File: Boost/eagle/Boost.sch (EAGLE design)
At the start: 17 parts, among them X1 22-23-2051

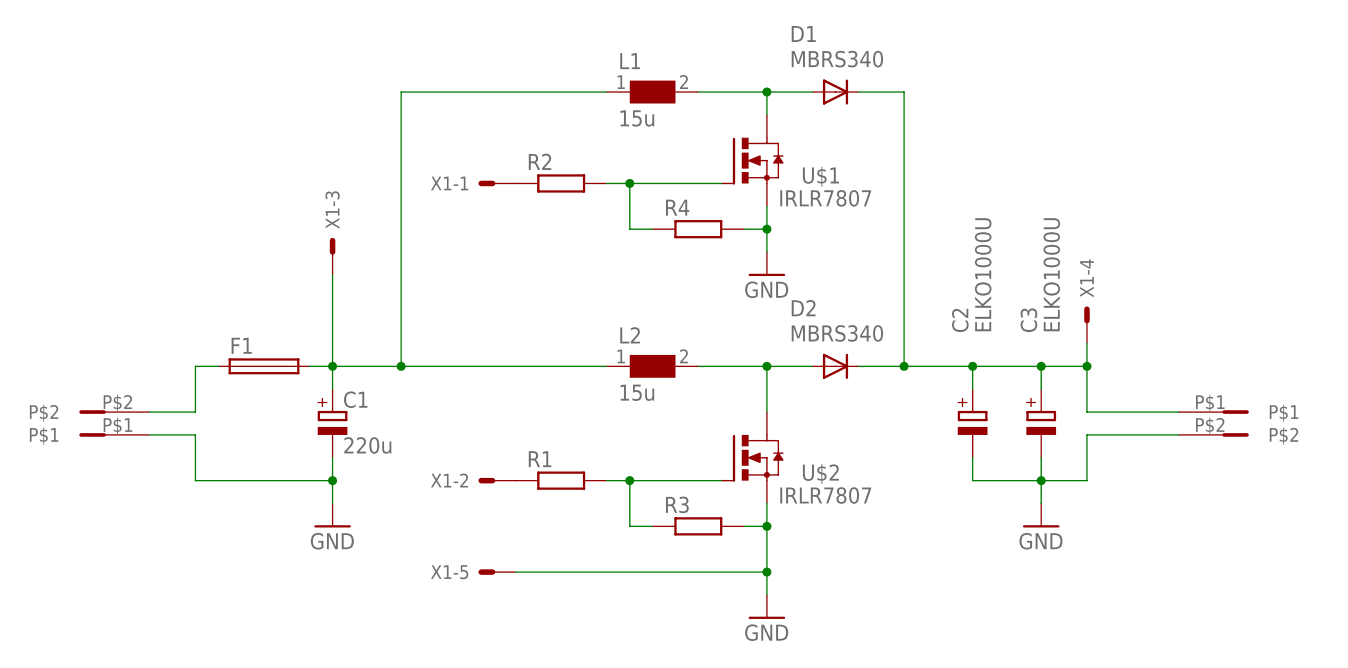
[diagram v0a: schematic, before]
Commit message: updated boost converter layout
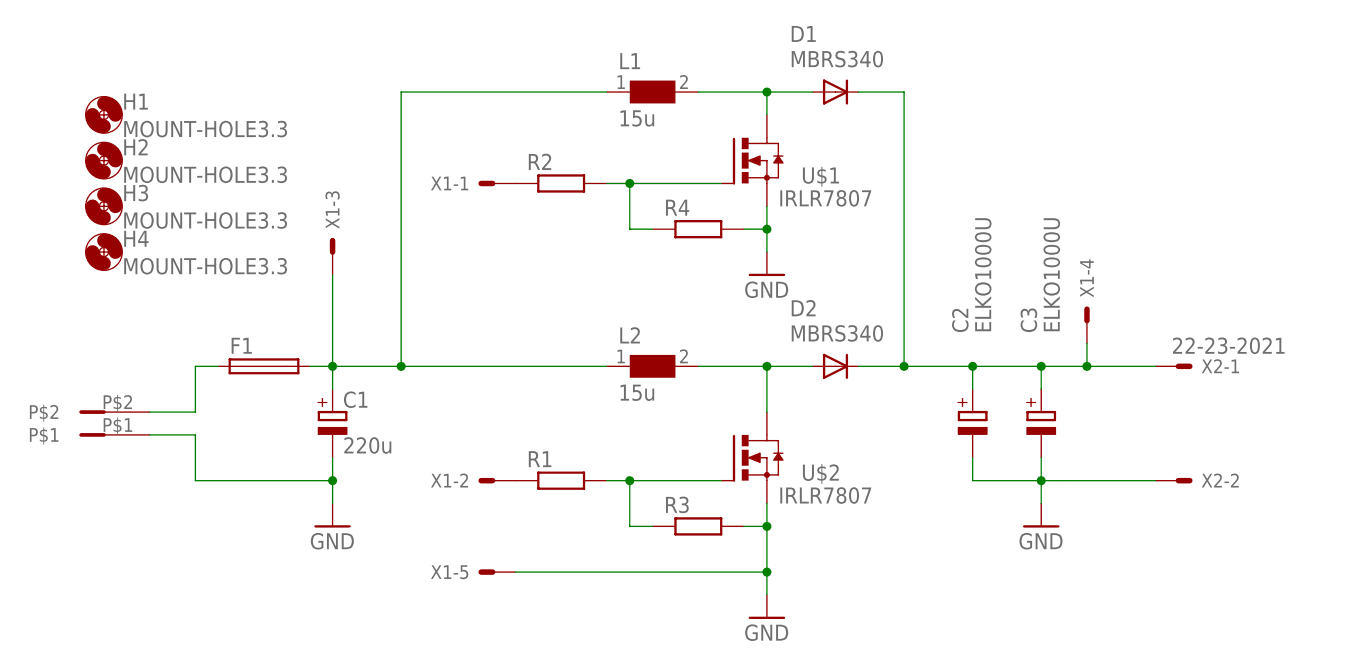
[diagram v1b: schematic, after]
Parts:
- removed U$4: RIACON-2, ppst002:RIACON-2
- added H1, H2, H3, H4: MOUNT-HOLE3.3, holes:MOUNT-HOLE3.3
- added X2: 22-23-2021, con-molex:22-23-2021
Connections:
- net GND: now also X2-2.S; no longer U$4.P$2
- net UOUT: now also X2-1.S; no longer U$4.P$1
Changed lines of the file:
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@@
 <grid distance="0.1" unitdist="inch" unit="inch" style="lines" multiple="1" display="no" altdistance="0.01" altunitdist="inch" altunit="inch"/>
 <layers>
-<layer number="1" name="Top" color="4" fill="1" visible="yes" active="no"/>
-<layer number="16" name="Bottom" color="1" fill="1" visible="yes" active="no"/>
-<layer number="17" name="Pads" color="2" fill="1" visible="yes" active="no"/>
-<layer number="18" name="Vias" color="2" fill="1" visible="yes" active="no"/>
-<layer number="19" name="Unrouted" color="6" fill="1" visible="yes" active="no"/>
-<layer number="20" name="Dimension" color="15" fill="1" visible="yes" active="no"/>
-<layer number="21" name="tPlace" color="7" fill="1" visible="yes" active="no"/>
-<layer number="22" name="bPlace" color="7" fill="1" visible="yes" active="no"/>
-<layer number="23" name="tOrigins" color="15" fill="1" visible="yes" active="no"/>
-<layer number="24" name="bOrigins" color="15" fill="1" visible="yes" active="no"/>
-<layer number="25" name="tNames" color="7" fill="1" visible="yes" active="no"/>
-<layer number="26" name="bNames" color="7" fill="1" visible="yes" active="no"/>
-<layer number="27" name="tValues" color="7" fill="1" visible="yes" active="no"/>
-<layer number="28" name="bValues" color="7" fill="1" visible="yes" active="no"/>
+<layer number="1" name="Top" color="4" fill="1" visible="no" active="no"/>
+<layer number="16" name="Bottom" color="1" fill="1" visible="no" active="no"/>
+<layer number="17" name="Pads" color="2" fill="1" visible="no" active="no"/>
+<layer number="18" name="Vias" color="2" fill="1" visible="no" active="no"/>
+<layer number="19" name="Unrouted" color="6" fill="1" visible="no" active="no"/>
+<layer number="20" name="Dimension" color="15" fill="1" visible="no" active="no"/>
+<layer number="21" name="tPlace" color="7" fill="1" visible="no" active="no"/>
+<layer number="22" name="bPlace" color="7" fill="1" visible="no" active="no"/>
+<layer number="23" name="tOrigins" color="15" fill="1" visible="no" active="no"/>
+<layer number="24" name="bOrigins" color="15" fill="1" visible="no" active="no"/>
+<layer number="25" name="tNames" color="7" fill="1" visible="no" active="no"/>
+<layer number="26" name="bNames" color="7" fill="1" visible="no" active="no"/>
+<layer number="27" name="tValues" color="7" fill="1" visible="no" active="no"/>
+<layer number="28" name="bValues" color="7" fill="1" visible="no" active="no"/>
 <layer number="29" name="tStop" color="7" fill="3" visible="no" active="no"/>
 <layer number="30" name="bStop" color="7" fill="6" visible="no" active="no"/>
@@
 <layer number="35" name="tGlue" color="7" fill="4" visible="no" active="no"/>
 <layer number="36" name="bGlue" color="7" fill="5" visible="no" active="no"/>
-<layer number="37" name="tTest" color="7" fill="1" visible="yes" active="no"/>
-<layer number="38" name="bTest" color="7" fill="1" visible="yes" active="no"/>
+<layer number="37" name="tTest" color="7" fill="1" visible="no" active="no"/>
+<layer number="38" name="bTest" color="7" fill="1" visible="no" active="no"/>
 <layer number="39" name="tKeepout" color="4" fill="11" visible="no" active="no"/>
 <layer number="40" name="bKeepout" color="1" fill="11" visible="no" active="no"/>
@@
 <layer number="44" name="Drills" color="7" fill="1" visible="no" active="no"/>
 <layer number="45" name="Holes" color="7" fill="1" visible="no" active="no"/>
-<layer number="46" name="Milling" color="3" fill="1" visible="yes" active="no"/>
-<layer number="47" name="Measures" color="7" fill="1" visible="yes" active="no"/>
-<layer number="48" name="Document" color="7" fill="1" visible="yes" active="no"/>
-<layer number="49" name="Reference" color="7" fill="1" visible="yes" active="no"/>
-<layer number="50" name="dxf" color="7" fill="1" visible="yes" active="no"/>
-<layer number="51" name="tDocu" color="7" fill="1" visible="yes" active="no"/>
-<layer number="52" name="bDocu" color="7" fill="1" visible="yes" active="no"/>
-<layer number="53" name="tGND_GNDA" color="7" fill="9" visible="yes" active="no"/>
-<layer number="54" name="bGND_GNDA" color="1" fill="9" visible="yes" active="no"/>
-<layer number="56" name="wert" color="7" fill="1" visible="yes" active="no"/>
-<layer number="60" name="Board" color="7" fill="1" visible="yes" active="no"/>
+<layer number="46" name="Milling" color="3" fill="1" visible="no" active="no"/>
+<layer number="47" name="Measures" color="7" fill="1" visible="no" active="no"/>
+<layer number="48" name="Document" color="7" fill="1" visible="no" active="no"/>
+<layer number="49" name="Reference" color="7" fill="1" visible="no" active="no"/>
+<layer number="50" name="dxf" color="7" fill="1" visible="no" active="no"/>
+<layer number="51" name="tDocu" color="7" fill="1" visible="no" active="no"/>
+<layer number="52" name="bDocu" color="7" fill="1" visible="no" active="no"/>
+<layer number="53" name="tGND_GNDA" color="7" fill="9" visible="no" active="no"/>
+<layer number="54" name="bGND_GNDA" color="1" fill="9" visible="no" active="no"/>
+<layer number="56" name="wert" color="7" fill="1" visible="no" active="no"/>
+<layer number="60" name="Board" color="7" fill="1" visible="no" active="no"/>
 <layer number="90" name="Modules" color="5" fill="1" visible="yes" active="yes"/>
 <layer number="91" name="Nets" color="2" fill="1" visible="yes" active="yes"/>
@@
 <part name="R3" library="resistor" deviceset="R-EU_" device="MELF0204W"/>
 <part name="R4" library="resistor" deviceset="R-EU_" device="MELF0204W"/>
-<part name="U$4" library="ppst002" deviceset="RIACON-2" device=""/>
 <part name="C2" library="ppst002" deviceset="ELKO1000U" device=""/>
+<part name="X2" library="con-molex" deviceset="22-23-2021" device=""/>
+<part name="H1" library="holes" deviceset="MOUNT-HOLE" device="3.3"/>
+<part name="H2" library="holes" deviceset="MOUNT-HOLE" device="3.3"/>
+<part name="H3" library="holes" deviceset="MOUNT-HOLE" device="3.3"/>
+<part name="H4" library="holes" deviceset="MOUNT-HOLE" device="3.3"/>
 </parts>
 <sheets>
@@
 <instance part="R3" gate="G$1" x="71.12" y="10.16"/>
 <instance part="R4" gate="G$1" x="71.12" y="43.18"/>
-<instance part="U$4" gate="G$1" x="127" y="20.32"/>
 <instance part="C2" gate="G$1" x="101.6" y="20.32" smashed="yes">
 <attribute name="NAME" x="101.1174" y="31.623" size="1.778" layer="95" rot="R90"/>
 <attribute name="VALUE" x="103.6574" y="31.623" size="1.778" layer="96" rot="R90"/>
 </instance>
+<instance part="X2" gate="-1" x="124.46" y="27.94"/>
+<instance part="X2" gate="-2" x="124.46" y="15.24"/>
+<instance part="H1" gate="G$1" x="5.08" y="55.88"/>
+<instance part="H2" gate="G$1" x="5.08" y="50.8"/>
+<instance part="H3" gate="G$1" x="5.08" y="45.72"/>
+<instance part="H4" gate="G$1" x="5.08" y="40.64"/>
 </instances>
 <busses>
@@
 <pinref part="C3" gate="G$1" pin="-"/>
 <pinref part="GND3" gate="1" pin="GND"/>
-<pinref part="U$4" gate="G$1" pin="P$2"/>
-<wire x1="124.46" y1="20.32" x2="114.3" y2="20.32" width="0.1524" layer="91"/>
-<wire x1="114.3" y1="20.32" x2="114.3" y2="15.24" width="0.1524" layer="91"/>
-<wire x1="114.3" y1="15.24" x2="109.22" y2="15.24" width="0.1524" layer="91"/>
+<wire x1="121.92" y1="15.24" x2="111.76" y2="15.24" width="0.1524" layer="91"/>
 <pinref part="C2" gate="G$1" pin="-"/>
+<wire x1="111.76" y1="15.24" x2="109.22" y2="15.24" width="0.1524" layer="91"/>
 <wire x1="109.22" y1="15.24" x2="109.22" y2="12.7" width="0.1524" layer="91"/>
 <wire x1="101.6" y1="17.78" x2="101.6" y2="15.24" width="0.1524" layer="91"/>
@@
 <wire x1="109.22" y1="15.24" x2="109.22" y2="17.78" width="0.1524" layer="91"/>
 <junction x="109.22" y="15.24"/>
+<pinref part="X2" gate="-2" pin="S"/>
 </segment>
 <segment>
@@
 <wire x1="109.22" y1="25.4" x2="109.22" y2="27.94" width="0.1524" layer="91"/>
 <wire x1="109.22" y1="27.94" x2="114.3" y2="27.94" width="0.1524" layer="91"/>
-<pinref part="U$4" gate="G$1" pin="P$1"/>
 <wire x1="114.3" y1="30.48" x2="114.3" y2="27.94" width="0.1524" layer="91"/>
-<wire x1="114.3" y1="27.94" x2="114.3" y2="22.86" width="0.1524" layer="91"/>
-<wire x1="114.3" y1="22.86" x2="124.46" y2="22.86" width="0.1524" layer="91"/>
+<wire x1="114.3" y1="27.94" x2="121.92" y2="27.94" width="0.1524" layer="91"/>
 <pinref part="C2" gate="G$1" pin="+"/>
 <junction x="101.6" y="27.94"/>
 <junction x="109.22" y="27.94"/>
 <junction x="114.3" y="27.94"/>
-</segment>
-</net>
+<pinref part="X2" gate="-1" pin="S"/>
+</segment>
+</net>

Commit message: boost: change resistor values
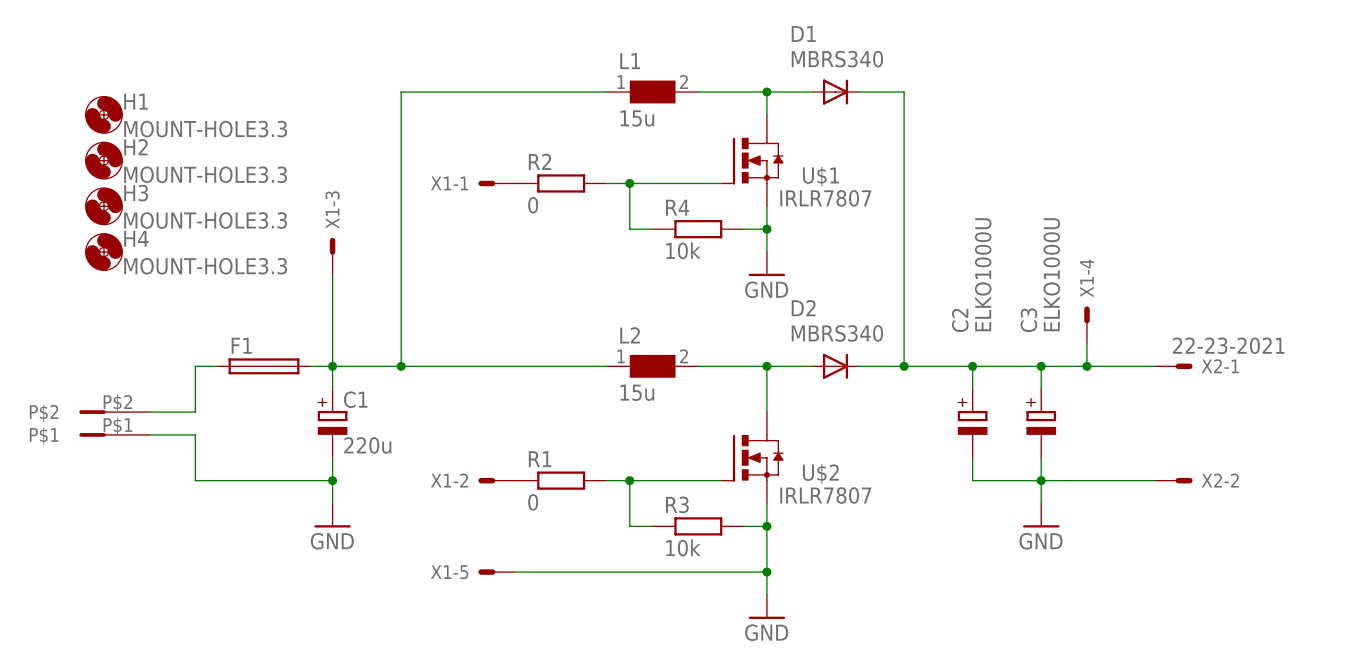
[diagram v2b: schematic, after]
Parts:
- R1, R2: value (none) -> 0
- R3, R4: value (none) -> 10k
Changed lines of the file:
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@@
 <part name="F1" library="fuse" deviceset="SH22,5" device=""/>
 <part name="X1" library="con-molex" deviceset="22-23-2051" device=""/>
-<part name="R1" library="resistor" deviceset="R-EU_" device="MELF0204W"/>
-<part name="R2" library="resistor" deviceset="R-EU_" device="MELF0204W"/>
-<part name="R3" library="resistor" deviceset="R-EU_" device="MELF0204W"/>
-<part name="R4" library="resistor" deviceset="R-EU_" device="MELF0204W"/>
+<part name="R1" library="resistor" deviceset="R-EU_" device="MELF0204W" value="0"/>
+<part name="R2" library="resistor" deviceset="R-EU_" device="MELF0204W" value="0"/>
+<part name="R3" library="resistor" deviceset="R-EU_" device="MELF0204W" value="10k"/>
+<part name="R4" library="resistor" deviceset="R-EU_" device="MELF0204W" value="10k"/>
 <part name="C2" library="ppst002" deviceset="ELKO1000U" device=""/>
 <part name="X2" library="con-molex" deviceset="22-23-2021" device=""/>
